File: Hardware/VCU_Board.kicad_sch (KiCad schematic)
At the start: 27 parts, among them J1 THROTTLE, J2 48V Battery, K1 CONTACTOR, K2 RELAY_PRECHARGE, Q1 MOSFET_CONTACTOR, Q2 MOSFET_PRECHARGE, SW1 SW_START, SW3 SW_DIRECTION, SW4 SW_BRAKE, SW5 SW_PUSH_EMERGENCY_NO, SW6 SW_PUSH_EMERGENCY_NC, U1 STM32G431RBTx, U2 SN65HVD230, U3 RPMH5.0-1.5

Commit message: Start adding ICM 20948
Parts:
- added J3: ICM-20948, Package_DFN_QFN:QFN-20-1EP_5x5mm_P0.65mm_EP3.35x3.35mm, symbol Connector_Generic:Conn_01x10
- added R8: 10k, Resistor_THT:R_Array_SIP4, symbol Device:R_US
- added R9: 33, symbol Device:R_US
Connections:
- net +3.3V: now also J3.1 (VCC), R8.1
- net GND: now also U3.A3 (GND), U3.A4 (GND), U3.B1 (GND), U3.B2 (GND), U3.B3 (GND), U3.B4 (GND), U3.C2 (GND), U3.C3 (GND), U3.C4 (GND), U3.D2 (GND), U3.D3 (GND), U3.D4 (GND), U3.D5 (GND), U3.E3 (GND), U3.E4 (GND), J3.2 (GND), J3.8 (FSY)
- net IMU_INT: now reaches U1.33 (PB11)
- net IMU_INT: now also J3.7 (INT)
- net SPI2_IMU_NCS: now reaches U1.34 (PB12)
- net SPI2_IMU_NCS: now also J3.5 (NCS), R8.2
- net SPI2_SCK: now reaches U1.35 (PB13)
- net SPI2_SCK: now also R9.1
- net SPI2_MISO: now reaches U1.36 (PB14)
- net SPI2_MISO: now also J3.6 (SDO)
- net SPI2_MOSI: now reaches U1.37 (PB15)
- net SPI2_MOSI: now also J3.4 (SDI)
- new net: J3.3 (SCLK), R9.2
- no-connect marks 0 -> 6
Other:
- company: (none) -> William Dubuc
- title: (none) -> Electric Go-Kart Main

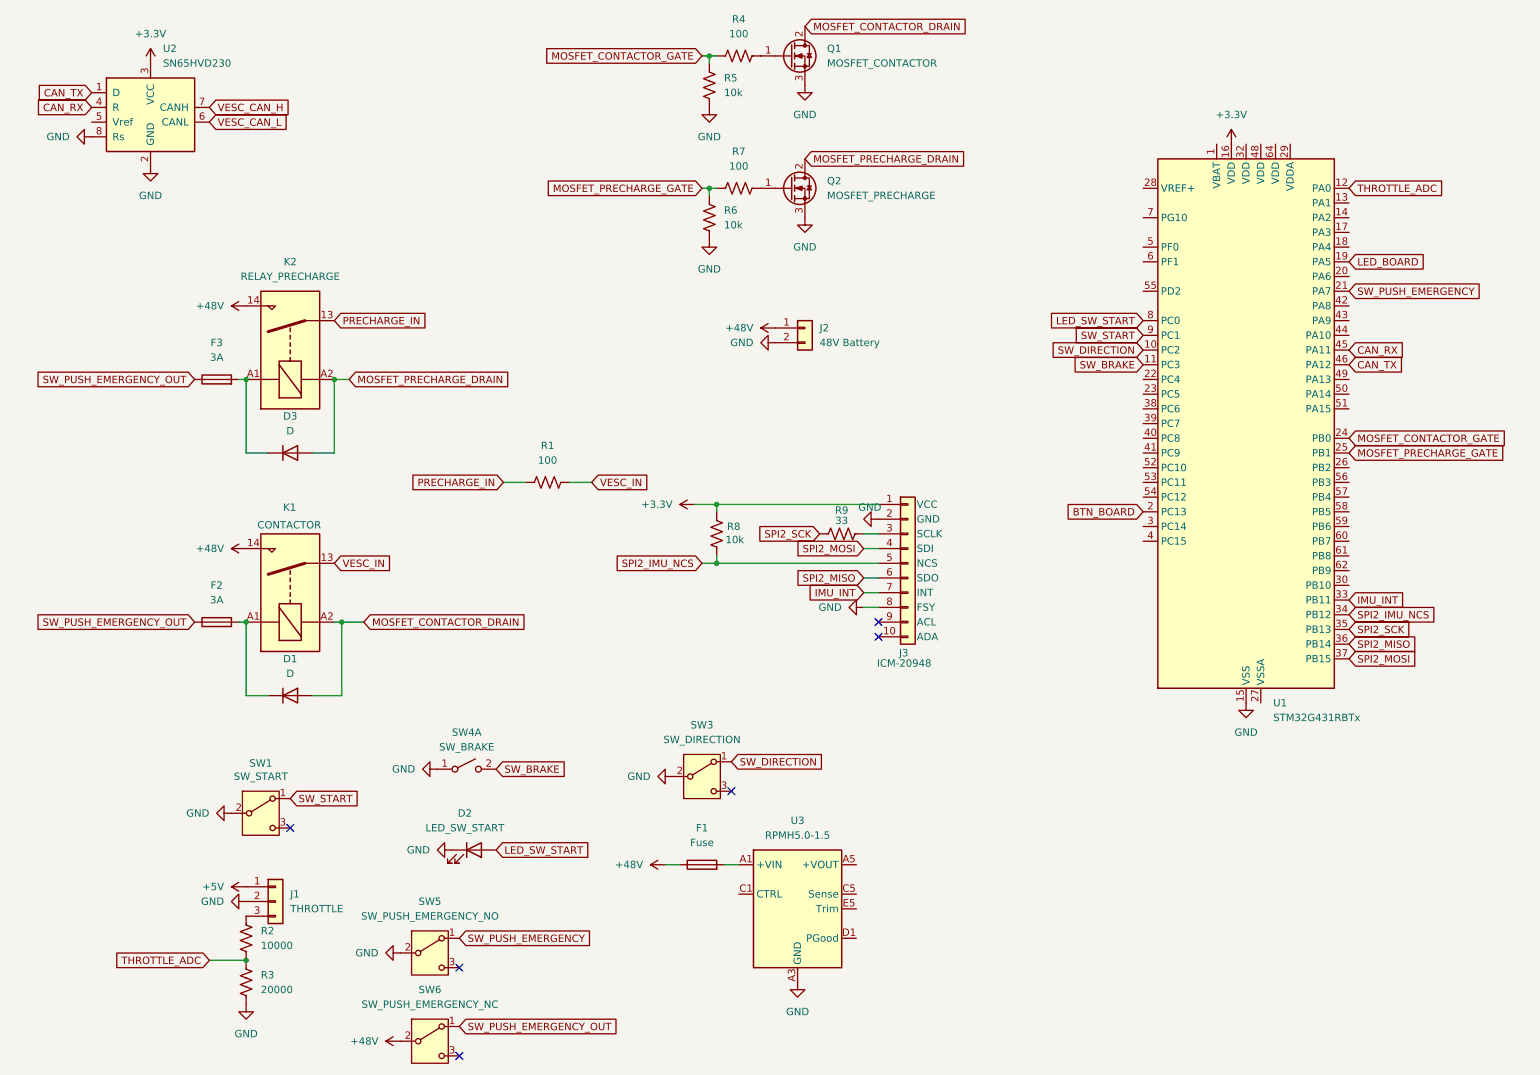
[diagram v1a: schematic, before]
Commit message: Start refactor VCU schema
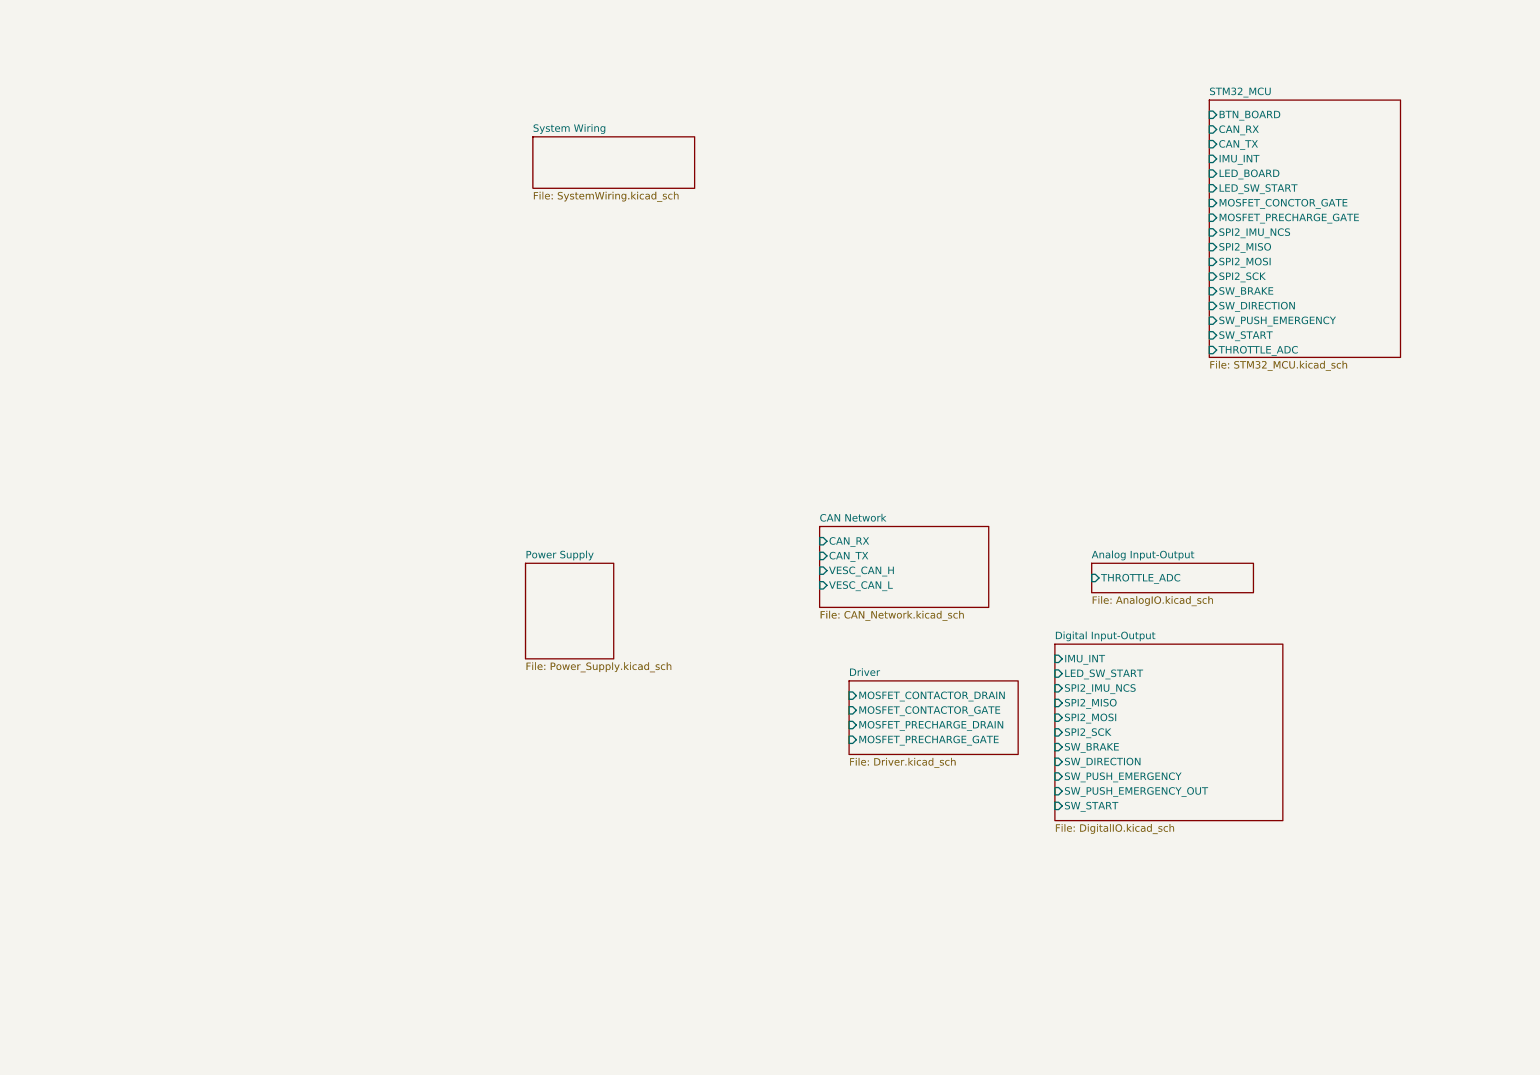
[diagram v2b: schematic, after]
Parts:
- removed D1, D3: D, symbol Device:D
- removed D2: LED_SW_START, Package_SON:WSON-8-1EP_6x5mm_P1.27mm_EP3.4x4mm, symbol Device:LED
- removed F1: Fuse, Package_LCC:PLCC-84_29.3x29.3mm_P1.27mm, symbol Device:Fuse
- removed F2, F3: 3A, symbol Device:Fuse
- removed J1: THROTTLE, symbol Connector_Generic:Conn_01x03
- removed J2: 48V Battery, symbol Connector_Generic:Conn_01x02
- removed J3: ICM-20948, Package_DFN_QFN:QFN-20-1EP_5x5mm_P0.65mm_EP3.35x3.35mm, symbol Connector_Generic:Conn_01x10
- removed K1: CONTACTOR, Relay_THT:Relay_NCR_HHG1D-1, symbol Relay:Relay_SPST-NO
- removed K2: RELAY_PRECHARGE, Relay_THT:Relay_NCR_HHG1D-1, symbol Relay:Relay_SPST-NO
- removed Q1: MOSFET_CONTACTOR, Package_QFP:TQFP-44_10x10mm_P0.8mm, symbol Transistor_FET:Q_NMOS_GDS
- removed Q2: MOSFET_PRECHARGE, Package_QFP:TQFP-44_10x10mm_P0.8mm, symbol Transistor_FET:Q_NMOS_GDS
- removed R1: 100, symbol Device:R_US
- removed R2: 10000, Package_DFN_QFN:WDFN-10-1EP_3x3mm_P0.5mm_EP1.8x2.5mm, symbol Device:R_US
- removed R3: 20000, symbol Device:R_US
- removed R4, R7: 100, Package_DFN_QFN:WDFN-10-1EP_3x3mm_P0.5mm_EP1.8x2.5mm, symbol Device:R_US
- removed R5, R6: 10k, Package_DFN_QFN:WDFN-10-1EP_3x3mm_P0.5mm_EP1.8x2.5mm, symbol Device:R_US
- removed R8: 10k, Resistor_THT:R_Array_SIP4, symbol Device:R_US
- removed R9: 33, symbol Device:R_US
- removed SW1: SW_START, Button_Switch_SMD:Nidec_Copal_CAS-120A, symbol Switch:SW_SPDT
- removed SW3: SW_DIRECTION, Module:RaspberryPi_Pico_W_SMD_HandSolder, symbol Switch:SW_SPDT
- removed SW4: SW_BRAKE, Button_Switch_THT:SW_NKK_GW12LJP, symbol Switch:SW_DPST_x2
- removed SW5: SW_PUSH_EMERGENCY_NO, Module:RaspberryPi_Pico_W_SMD_HandSolder, symbol Switch:SW_SPDT
- removed SW6: SW_PUSH_EMERGENCY_NC, Module:RaspberryPi_Pico_W_SMD_HandSolder, symbol Switch:SW_SPDT
- removed U1: STM32G431RBTx, Package_QFP:LQFP-64_10x10mm_P0.5mm, symbol MCU_ST_STM32G4:STM32G431RBTx
- removed U2: SN65HVD230, Package_SO:SOIC-8_3.9x4.9mm_P1.27mm, symbol Interface_CAN_LIN:SN65HVD230
- removed U3: RPMH5.0-1.5, Converter_DCDC:Converter_DCDC_RECOM_RPMx.x-x.0, symbol Converter_DCDC:RPMH5.0-1.5
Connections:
- no-connect marks 6 -> 0
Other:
- added sheet Analog Input-Output (AnalogIO.kicad_sch)
- added sheet CAN Network (CAN_Network.kicad_sch)
- added sheet Digital Input-Output (DigitalIO.kicad_sch)
- added sheet Driver (Driver.kicad_sch)
- added sheet Power Supply (Power_Supply.kicad_sch)
- added sheet STM32_MCU (STM32_MCU.kicad_sch)
- added sheet System Wiring (SystemWiring.kicad_sch)

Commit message: Restructure VCU schema
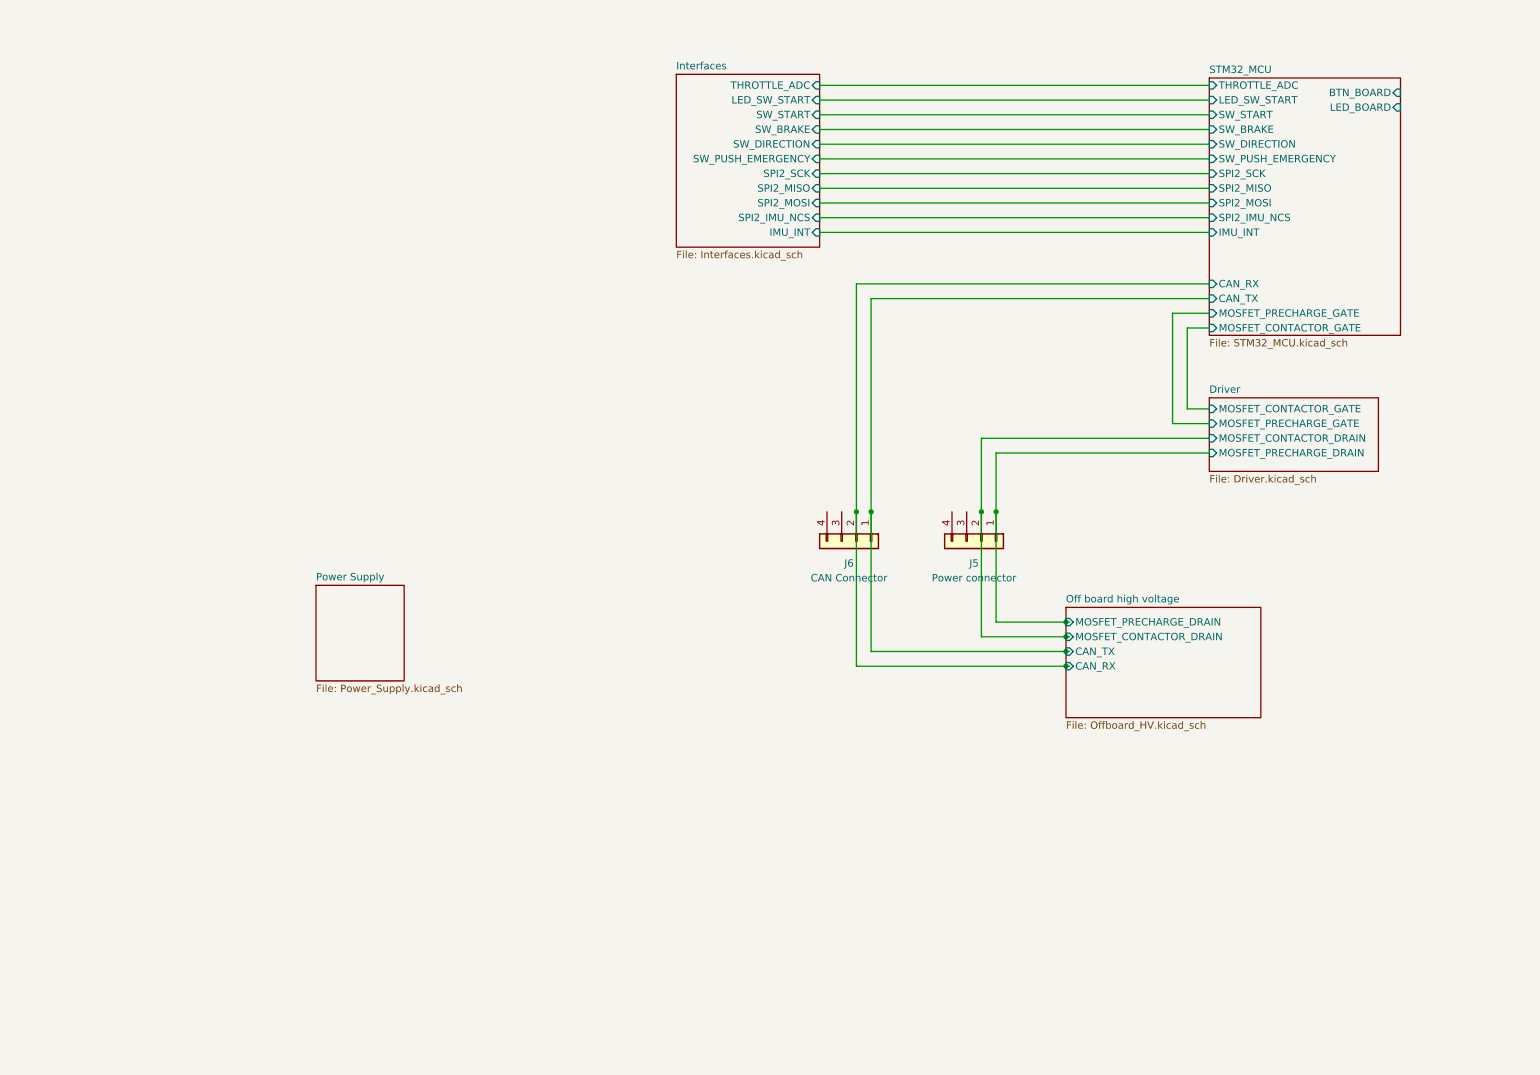
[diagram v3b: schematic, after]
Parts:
- added J5: Power connector, Oscillator:Oscillator_DIP-14, symbol Connector_Generic:Conn_01x04
- added J6: CAN Connector, Oscillator:Oscillator_DIP-14, symbol Connector_Generic:Conn_01x04
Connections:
- net Driver/MOSFET_CONTACTOR_DRAIN: now also J5.2 (Pin_2)
- net Driver/MOSFET_PRECHARGE_DRAIN: now also J5.1 (Pin_1)
- new net Off board high voltage/CAN_RX: J6.2 (Pin_2)
- new net Off board high voltage/CAN_TX: J6.1 (Pin_1)
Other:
- removed sheet Analog Input-Output
- removed sheet CAN Network
- removed sheet Digital Input-Output
- removed sheet System Wiring
- added sheet Interfaces (Interfaces.kicad_sch)
- added sheet Off board high voltage (Offboard_HV.kicad_sch)
- sheet STM32_MCU ports: added MOSFET_CONTACTOR_GATE; removed MOSFET_CONCTOR_GATE

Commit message: Set footprint + excludes
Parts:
- J5, J6: footprint Oscillator:Oscillator_DIP-14 -> TerminalBlock_Phoenix:TerminalBlock_Phoenix_MPT-0,5-4-2.54_1x04_P2.54mm_Horizontal
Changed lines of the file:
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@@
 			)
 		)
-		(property "Footprint" "Oscillator:Oscillator_DIP-14"
+		(property "Footprint" "TerminalBlock_Phoenix:TerminalBlock_Phoenix_MPT-0,5-4-2.54_1x04_P2.54mm_Horizontal"
 			(at 185.42 105.41 0)
 			(hide yes)
@@
 			)
 		)
-		(property "Footprint" "Oscillator:Oscillator_DIP-14"
+		(property "Footprint" "TerminalBlock_Phoenix:TerminalBlock_Phoenix_MPT-0,5-4-2.54_1x04_P2.54mm_Horizontal"
 			(at 163.83 105.41 0)
 			(hide yes)
